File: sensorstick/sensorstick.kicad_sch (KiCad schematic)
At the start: 8 parts, among them J1 U217-04XN-XXR84, U1 ESP32-C3_SUPERMINI, U2 SCD40 CO2 module, U3 GY-SGP30

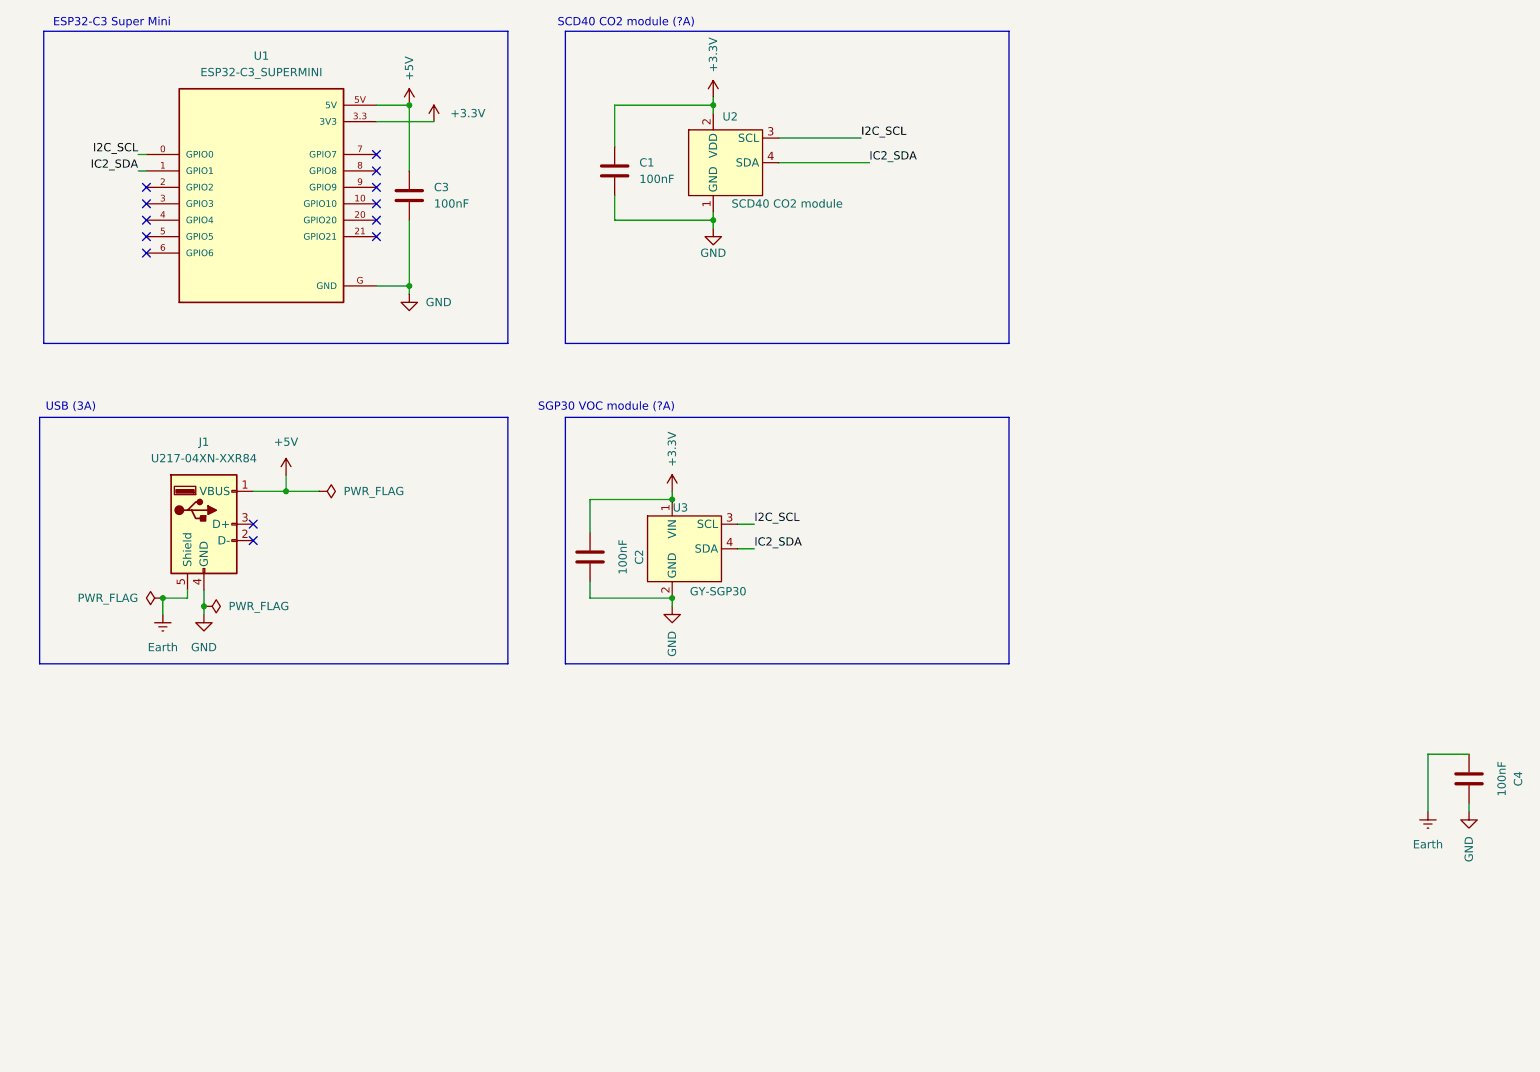
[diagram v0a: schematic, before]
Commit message: minimal desin with new sensor
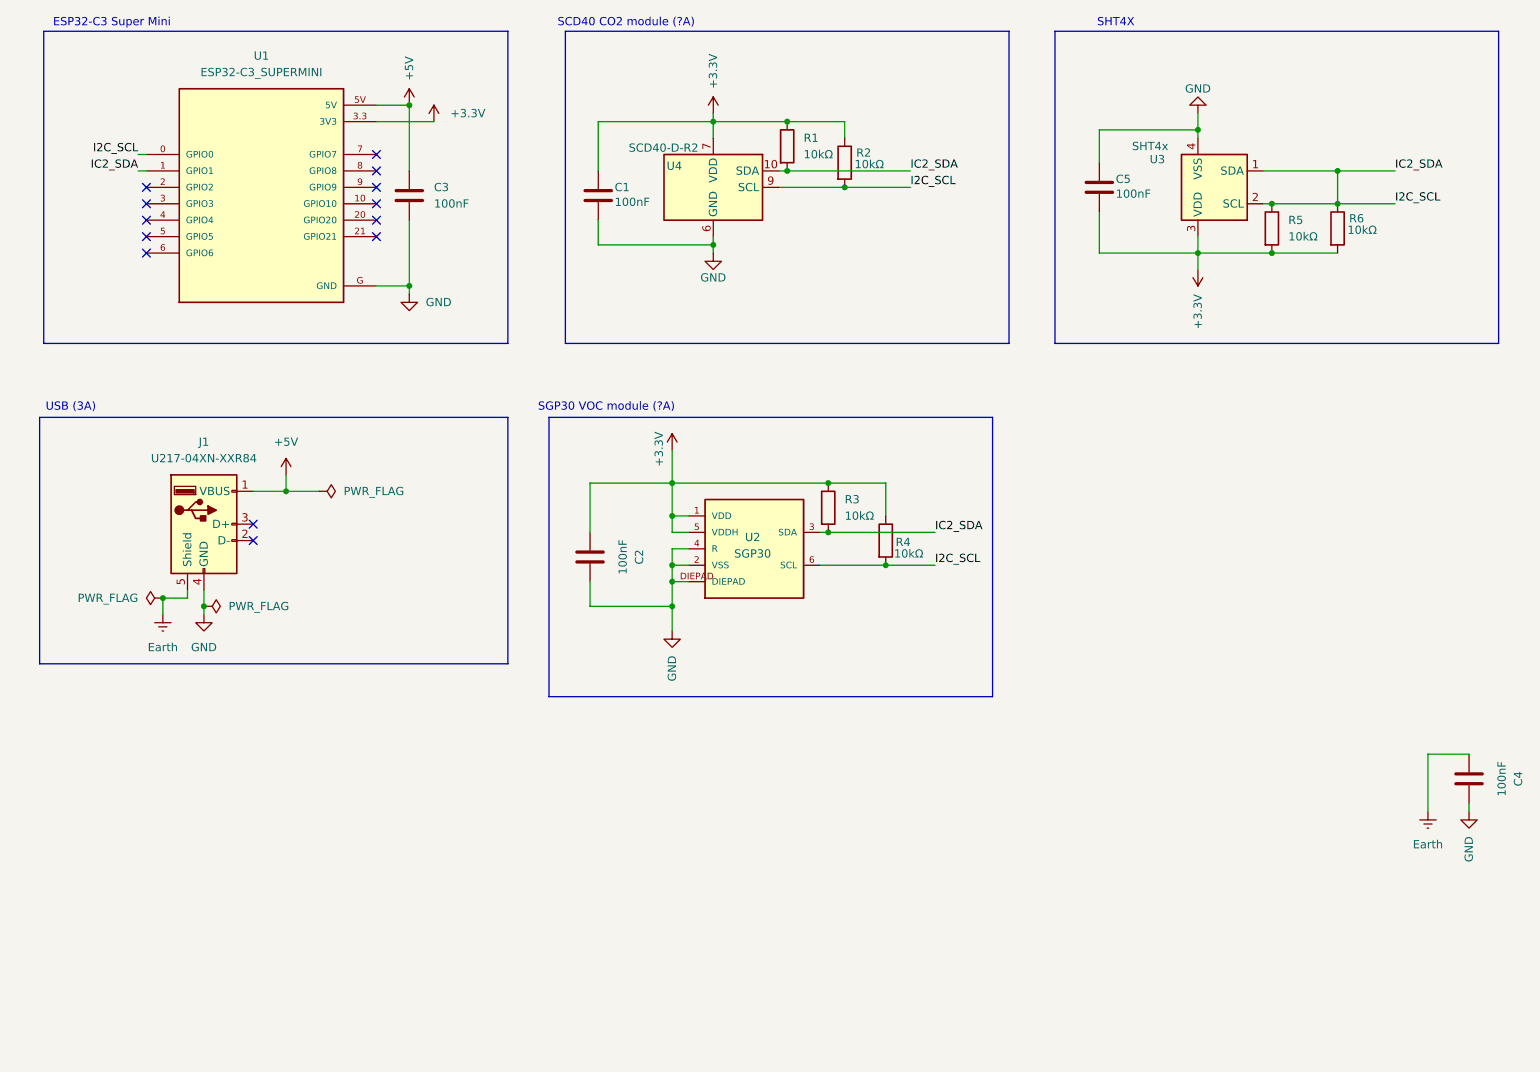
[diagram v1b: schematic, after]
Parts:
- removed U2: SCD40 CO2 module, CustomLibrary:SCD40_CO2_module, symbol CustomSymbols:SCD40_CO2_module
- removed U3: GY-SGP30, CustomLibrary:GY-SGP30_VOC_module, symbol CustomSymbols:GY-SGP30_VOC_module
- added C5: 100nF, Capacitor_SMD:C_0603_1608Metric, symbol Device:C
- added R1, R2, R3, R4, R5, R6: 10kΩ, Resistor_SMD:R_0603_1608Metric, symbol Device:R
- added U2: SGP30, SGP30:SGP30, symbol SGP30:SGP30
- added U3: SHT4x, Sensor_Humidity:Sensirion_DFN-4_1.5x1.5mm_P0.8mm_SHT4x_NoCentralPad, symbol Sensor_Humidity:SHT4x
- added U4: SCD40-D-R2, Sensor:Sensirion_SCD4x-1EP_10.1x10.1mm_P1.25mm_EP4.8x4.8mm, symbol Sensor_Gas:SCD40-D-R2
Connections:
- net IC2_SDA is gone; now on net I2C_SCL: U1.1 (GPIO1)
- net +3.3V: now also C5.1, R1.1, R2.1, R3.1, R4.1, R5.2, R6.2, U2.1 (VDD), U2.5 (VDDH), U3.3 (VDD), U4.19 (VDD), U4.7 (VDD)
- net GND: now also C5.2, U2.2 (VSS), U2.4 (R), U2.DIEPAD, U3.4 (VSS), U4.20 (GND), U4.21 (GND), U4.6 (GND)
- net I2C_SCL: now also R1.2, R2.2, R3.2, R4.2, R5.1, R6.1, U2.3 (SDA), U2.6 (SCL), U3.1 (SDA), U3.2 (SCL), U4.10 (SDA), U4.9 (SCL)
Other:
- note added: "SHT4X"
- moved on the sheet: C1

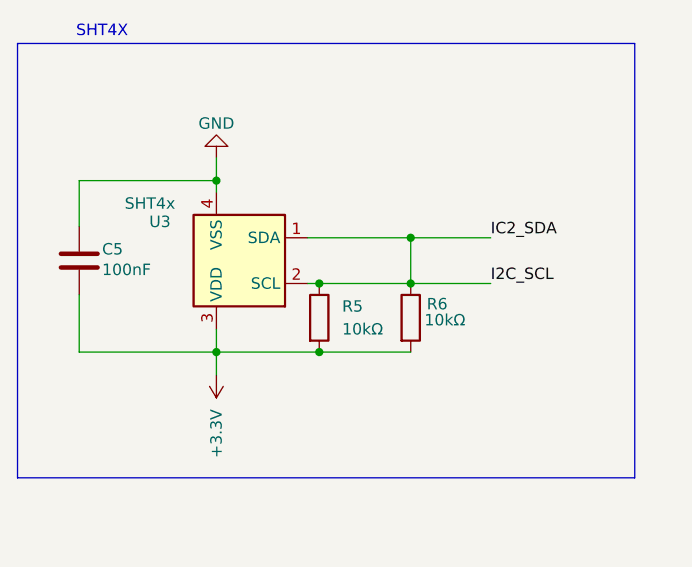
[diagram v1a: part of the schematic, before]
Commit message: finished first routing, open for review
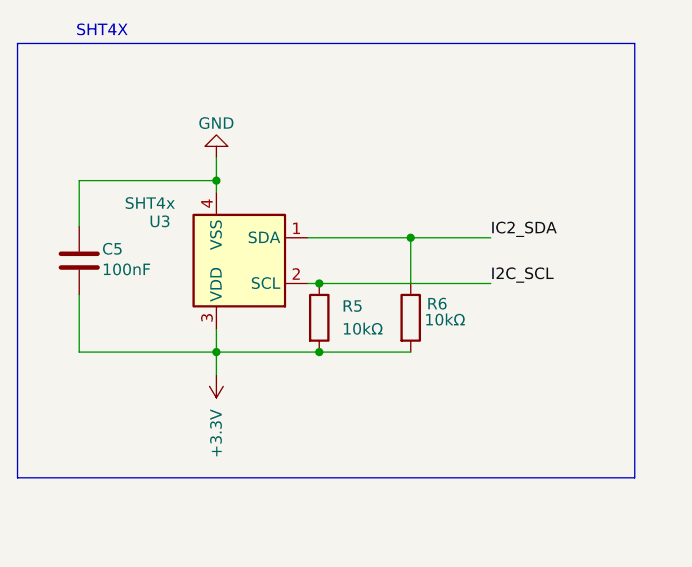
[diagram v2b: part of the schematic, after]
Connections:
- net I2C_SCL: no longer R1.2, R3.2, R6.1, U1.1 (GPIO1), U2.3 (SDA), U3.1 (SDA), U4.10 (SDA)
- new net IC2_SDA: R1.2, R3.2, R6.1, U1.1 (GPIO1), U2.3 (SDA), U3.1 (SDA), U4.10 (SDA)
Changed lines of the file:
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@@
-	)
-	(junction
-		(at 229.87 55.88)
-		(diameter 0)
-		(color 0 0 0 0)
 	)
 	(junction
@@
 	(wire
 		(pts
-			(xy 229.87 55.88) (xy 238.76 55.88)
+			(xy 219.71 55.88) (xy 238.76 55.88)
 		)
 		(stroke
@@
 		)
 		(stroke
-			(width 0)
-			(type default)
-		)
-	)
-	(wire
-		(pts
-			(xy 219.71 55.88) (xy 229.87 55.88)
-		)
-		(stroke

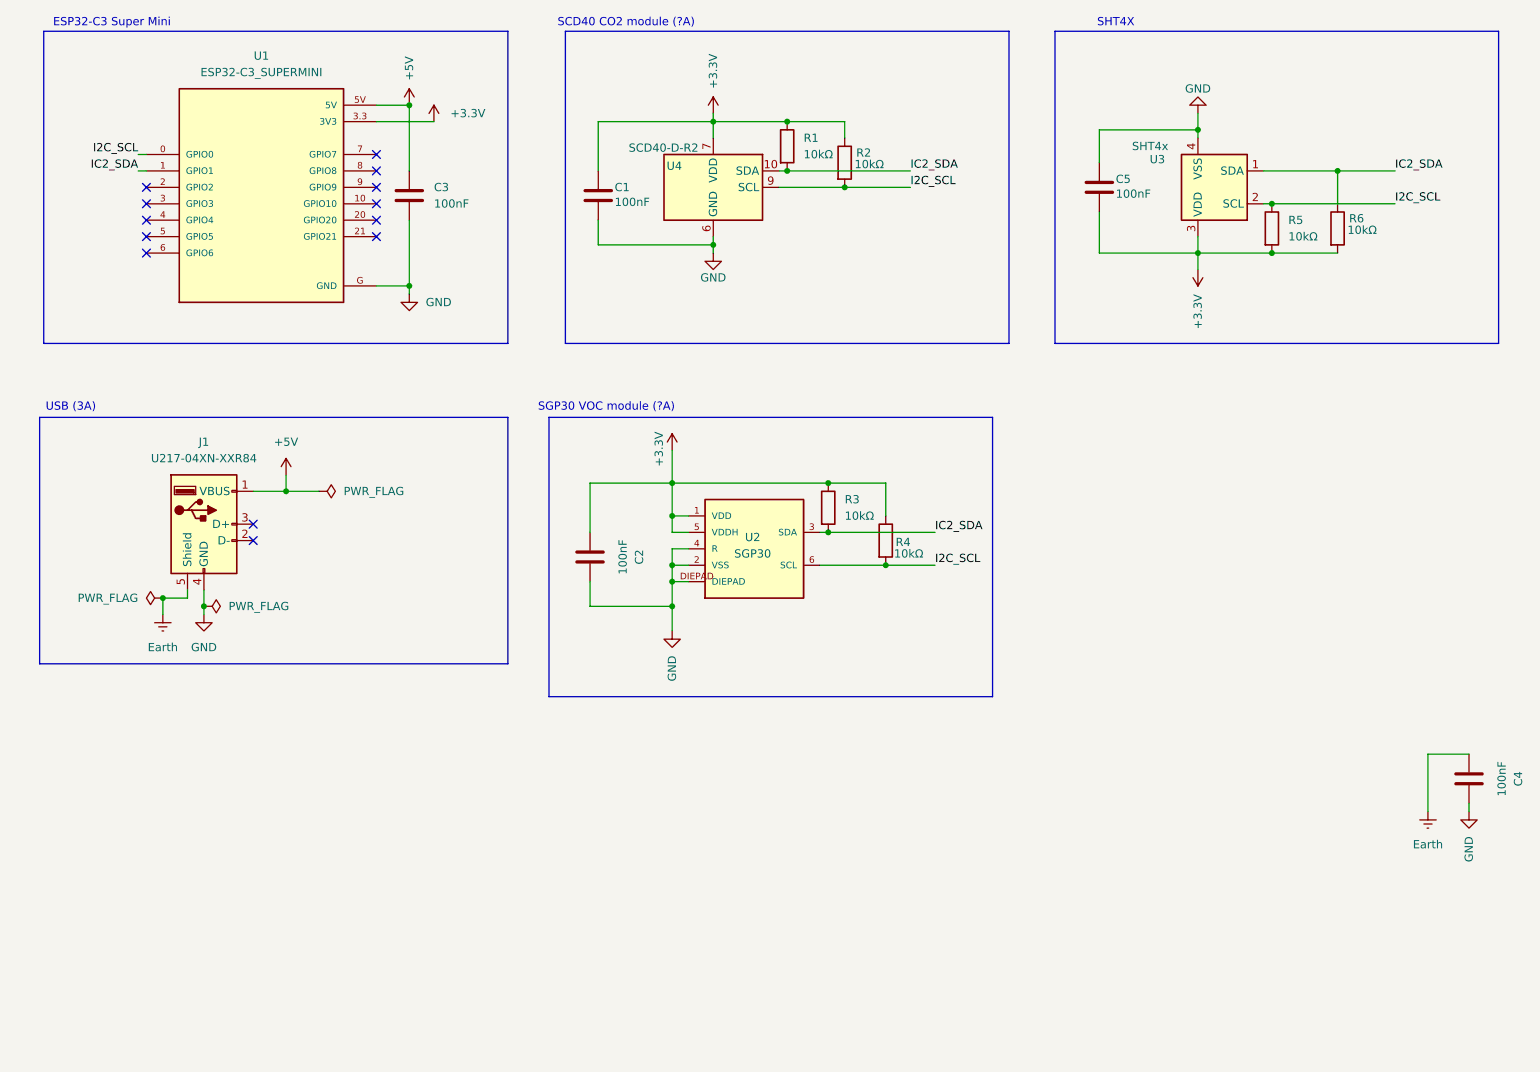
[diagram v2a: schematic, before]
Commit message: moved all parts on the backside for easyer asambly
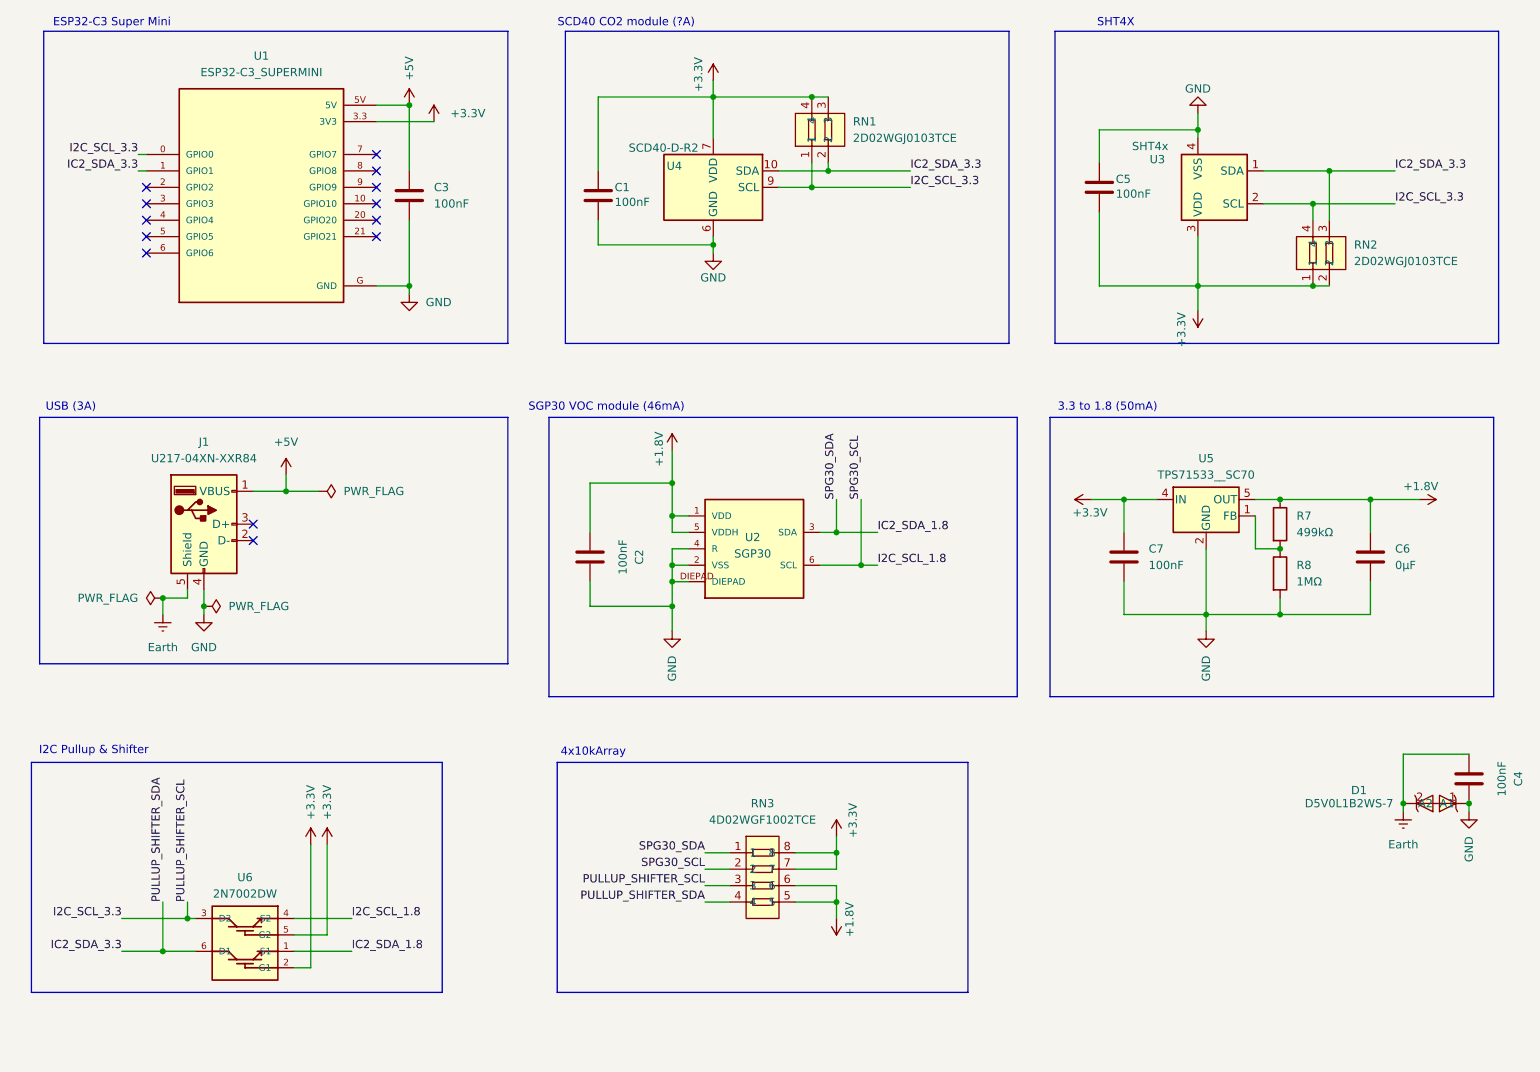
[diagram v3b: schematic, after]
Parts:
- removed R1, R2, R3, R4, R5, R6: 10kΩ, Resistor_SMD:R_0603_1608Metric, symbol Device:R
- added C6: 0μF, Capacitor_SMD:C_0603_1608Metric, symbol Device:C
- added C7: 100nF, Capacitor_SMD:C_0603_1608Metric, symbol Device:C
- added D1: D5V0L1B2WS-7, easyeda2kicad:SOD-323_L1.8-W1.3-LS2.5-BI, symbol easyeda2kicad:D5V0L1B2WS-7
- added R7: 499kΩ, Resistor_SMD:R_0603_1608Metric, symbol Device:R
- added R8: 1MΩ, Resistor_SMD:R_0603_1608Metric, symbol Device:R
- added RN1, RN2: 2D02WGJ0103TCE, easyeda2kicad:RES-ARRAY-SMD_0402-4P-L1.0-W1.0-BL, symbol easyeda2kicad:2D02WGJ0103TCE
- added RN3: 4D02WGF1002TCE, easyeda2kicad:RES-ARRAY-SMD_0402-8P-L2.0-W1.0-BL, symbol easyeda2kicad:4D02WGF1002TCE
- added U5: TPS71533__SC70, Package_TO_SOT_SMD:SOT-353_SC-70-5, symbol Regulator_Linear:TPS71533__SC70
- added U6: 2N7002DW, 2N7002DW:SOT363, symbol 2N7002DW:2N7002DW
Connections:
- net +3.3V: now also C7.1, RN1.3, RN1.4, RN2.1, RN2.2, RN3.7, RN3.8, U5.4 (IN), U6.2 (G1), U6.5 (G2); no longer C2.1, U2.1 (VDD), U2.5 (VDDH)
- net Earth: now also D1.2 (A1)
- net GND: now also C6.2, C7.2, D1.1 (A2), R8.2, U5.2 (GND)
- net I2C_SCL renamed I2C_SCL_3.3
- net I2C_SCL_3.3: now also RN1.1, RN2.4, RN3.3, U6.3 (D2); no longer U2.6 (SCL)
- net IC2_SDA renamed IC2_SDA_3.3
- net IC2_SDA_3.3: now also RN1.2, RN2.3, RN3.4, U6.6 (D1); no longer U2.3 (SDA)
- new net: R7.2, R8.1, U5.1 (FB)
- new net +1.8V: C2.1, C6.1, R7.1, RN3.5, RN3.6, U2.1 (VDD), U2.5 (VDDH), U5.5 (OUT)
- new net I2C_SCL_1.8: RN3.2, U2.6 (SCL), U6.4 (S2)
- new net IC2_SDA_1.8: RN3.1, U2.3 (SDA), U6.1 (S1)
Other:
- note added: "3.3 to 1.8 (50mA)"
- note added: "4x10kArray"
- note added: "I2C Pullup & Shifter"
- note added: "SGP30 VOC module (46mA)"
- note removed: "SGP30 VOC module (?A)"
